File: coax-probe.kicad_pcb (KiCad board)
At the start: 2 copper layers, 37.3 x 21 mm, 34 parts, among them J1 Conn_01x02, J2 Conn_Coaxial, J3 Conn_01x02, J4 Conn_01x03, J5 Conn_Coaxial, J6 Conn_01x02, U1 OPA690, U2 INA128, U3 OPA690, U4 CJ431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

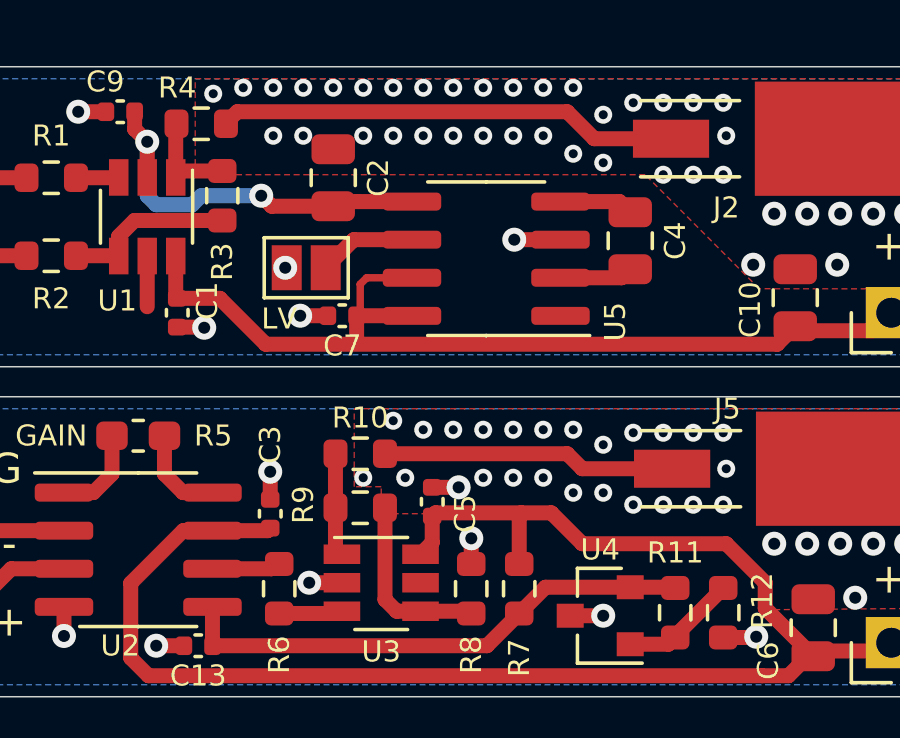
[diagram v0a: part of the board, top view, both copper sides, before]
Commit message: Fix 50-ohm trace width
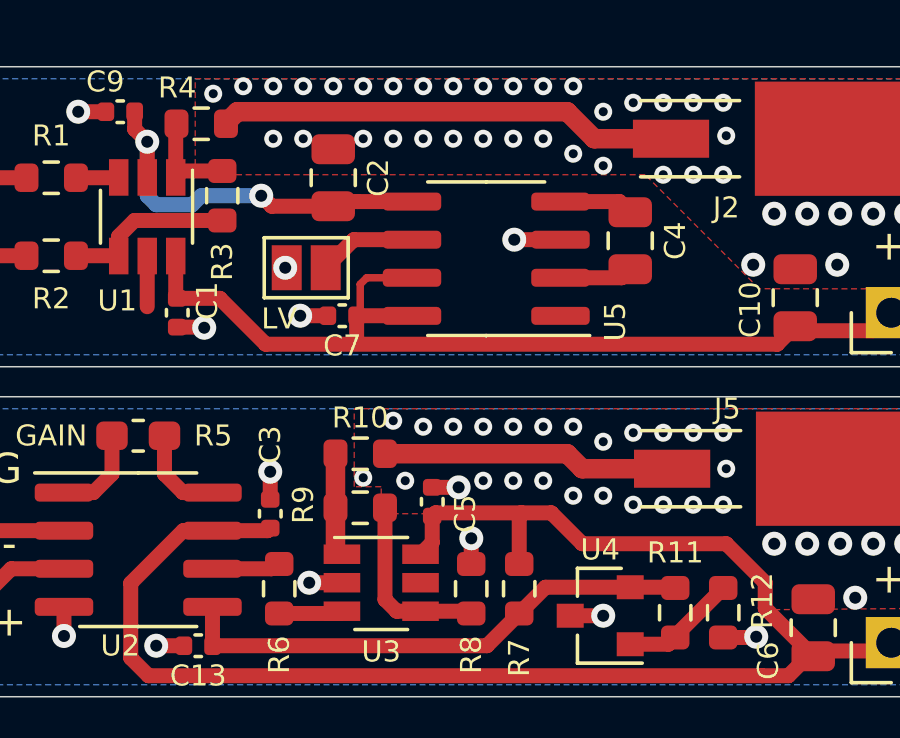
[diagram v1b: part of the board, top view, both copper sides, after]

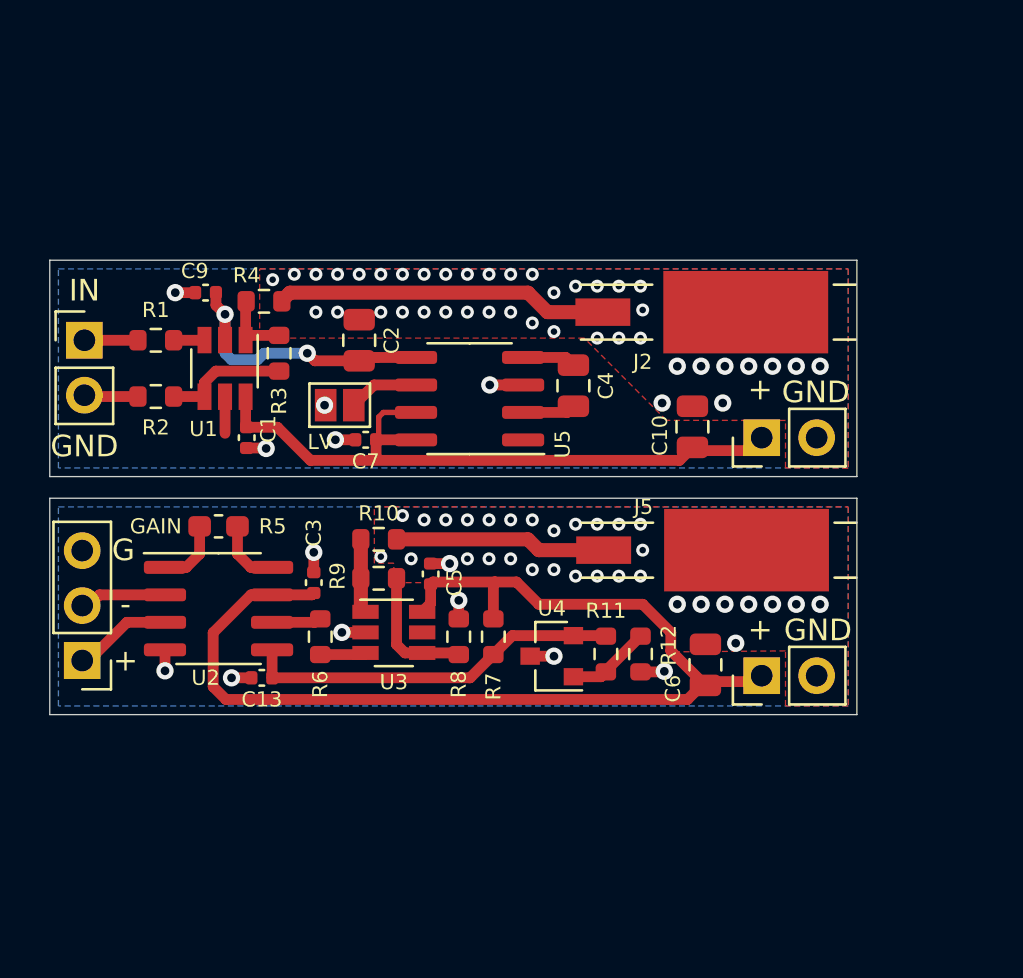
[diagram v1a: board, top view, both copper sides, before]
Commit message: Use SMA connectors
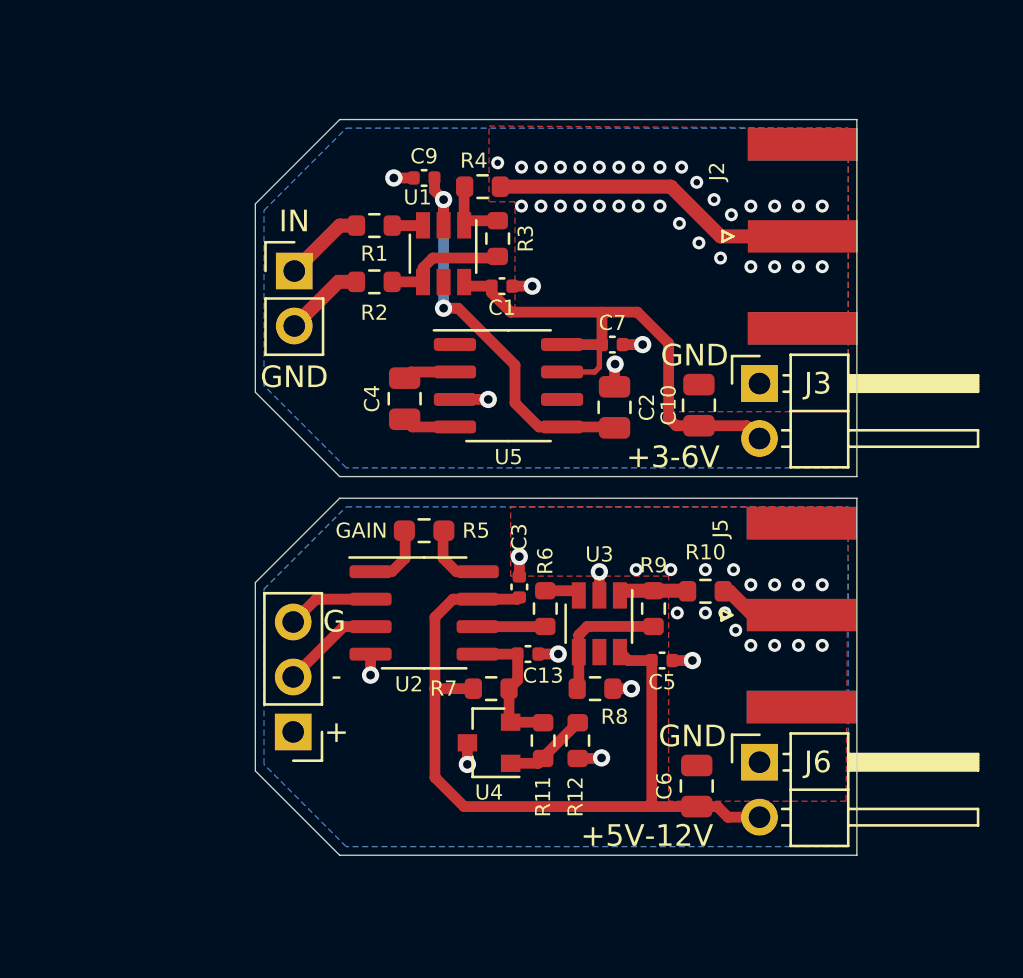
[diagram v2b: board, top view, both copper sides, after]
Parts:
- removed JP1: LV, Jumper:SolderJumper-2_P1.3mm_Open_Pad1.0x1.5mm
- J2, J5: value Conn_Coaxial -> SMA; footprint Beck:Coax_Cable_Solder -> Connector_Coaxial:SMA_Amphenol_132289_EdgeMount
- J3, J6: footprint Connector_PinHeader_2.54mm:PinHeader_1x02_P2.54mm_Vertical -> Connector_PinHeader_2.54mm:PinHeader_1x02_P2.54mm_Horizontal
- R12: value - -> DNP
- R5: value - -> DNP; footprint Capacitor_SMD:C_0603_1608Metric_Pad1.05x0.95mm_HandSolder -> Resistor_SMD:R_0603_1608Metric_Pad0.98x0.95mm_HandSolder
- moved R10 15.3 mm to (178.0, 75.3)
- moved C1 13.7 mm to (168.6, 61.2), turned to 0 degrees
- moved R9 12.8 mm to (175.6, 76.1), turned to 270 degrees
- moved C13 12.3 mm to (169.8, 78.2), turned to 0 degrees
- moved C7 12.2 mm to (173.7, 63.9), turned to 0 degrees
- moved C2 12.2 mm to (173.8, 66.8)
- moved C5 11.4 mm to (176.0, 78.5), turned to 0 degrees
- moved R1 11.4 mm to (162.7, 58.4)
- moved C9 11.4 mm to (165.0, 56.2)
- moved R2 11.4 mm to (162.7, 61.0)
- moved R3 11.4 mm to (168.4, 59.0)
- moved R4 11.4 mm to (167.7, 56.6)
- moved U1 11.4 mm to (165.9, 59.7)
- moved R6 10.5 mm to (170.6, 76.1), turned to 270 degrees
- moved J4 10.3 mm to (158.9, 81.8)
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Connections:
- J3 pad 1: VCC -> GND
- J3 pad 2: GND -> VCC
- J4 pad 1: /IN+ -> GND
- J4 pad 2: /IN- -> /IN+
- J4 pad 3: GND -> /IN-
- J6 pad 1: VCC -> GND
- J6 pad 2: GND -> VCC
- U5 pad 6: Net-(JP1-Pad1) -> (no net)
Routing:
- net VCC: track 84.4 -> 62.3 mm
- net REF: track 17.5 -> 6.70 mm
- net /OUTD: track 9.44 -> 4.08 mm
- net VSS: track 13.3 -> 18.6 mm
- net Net-(JP1-Pad1): track 3.26 -> 0.00 mm
- net GND: track 14.6 -> 16.9 mm, vias 87 -> 61
- net (no net): track 1.69 -> 0.00 mm
- net Net-(J1-Pad1): track 2.47 -> 3.74 mm
- net /INA: track 2.19 -> 3.13 mm
- net /OUT: track 15.5 -> 14.9 mm
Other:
- board size 37.3 x 21 mm -> 27.8 x 34 mm
- board text added: "220MHz 50Ω 1X Active Probe"
- board text added: "Active Differential Probe 1.2MHz (G=1) 50Ω"
- board text removed: "1.2MHz (G=1) 50Ω Active Differential Probe"
- board text removed: "2.5V−6V"
- board text removed: "220MHz 50Ω Active Probe"
- board text removed: "5V−12V"
- board text removed: "Solder LV for <3V"

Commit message: Tweak zones.
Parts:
- moved C10 0.20 mm to (177.5, 66.7)

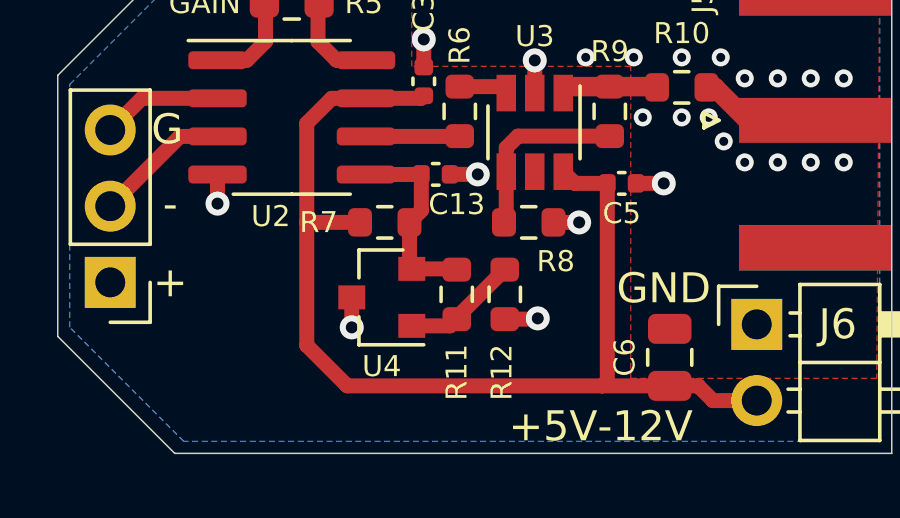
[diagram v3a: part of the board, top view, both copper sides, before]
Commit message: Space out Vref more
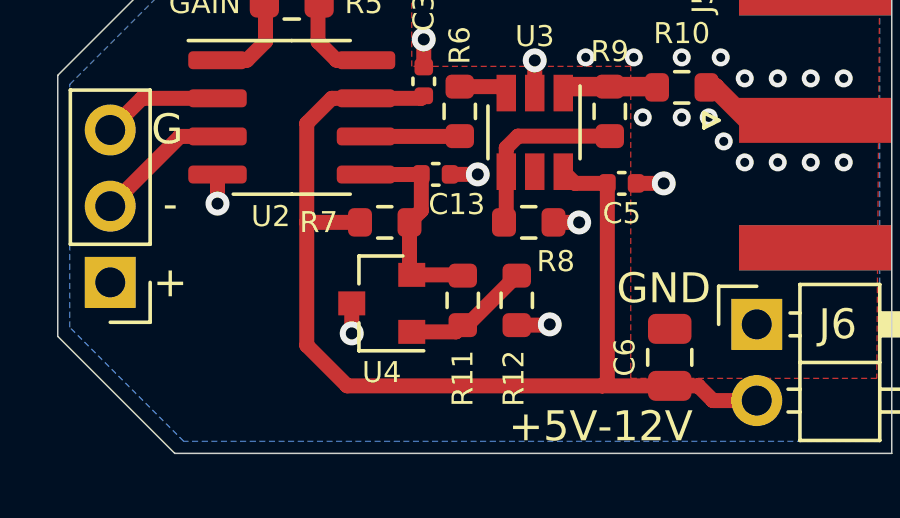
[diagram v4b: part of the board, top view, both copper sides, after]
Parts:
- moved R12 0.45 mm to (172.5, 82.4)
- moved R11 0.28 mm to (170.7, 82.4)
- moved U4 0.20 mm to (168.0, 82.5)
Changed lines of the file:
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@@
     (thickness 1.6)
     (drawings 28)
-    (tracks 190)
+    (tracks 191)
     (zones 0)
     (modules 33)
@@
   )
   (module Resistor_SMD:R_0603_1608Metric (layer F.Cu)
-    (at 172.1 82.2 270)
+    (at 172.5 82.4 270)
     (descr "Resistor SMD 0603 (1608 Metric), square (rectangular) end terminal, IPC_7351 nominal, (Body size source: IPC-SM-782 page 72, https://www.pcb-3d.com/wordpress/wp-content/uploads/ipc-sm-782a_amendment_1_and_2.pdf), generated with kicad-footprint-generator")
     (tags resistor)
@@
   )
   (module Resistor_SMD:R_0603_1608Metric (layer F.Cu)
-    (at 170.5 82.2 270)
+    (at 170.7 82.4 270)
     (descr "Resistor SMD 0603 (1608 Metric), square (rectangular) end terminal, IPC_7351 nominal, (Body size source: IPC-SM-782 page 72, https://www.pcb-3d.com/wordpress/wp-content/uploads/ipc-sm-782a_amendment_1_and_2.pdf), generated with kicad-footprint-generator")
     (tags resistor)
@@
   )
   (module Package_TO_SOT_SMD:SOT-23 (layer F.Cu)
-    (at 168 82.3 180)
+    (at 168 82.5 180)
     (descr "SOT-23, Standard")
     (tags SOT-23)
@@
   (via (at 173.1 74.399998) (size 0.8) (drill 0.4) (layers F.Cu B.Cu) (net 1))
   (segment (start 173.1 75.49) (end 173.1 74.399998) (width 0.5) (layer F.Cu) (net 1))
-  (via (at 173.2 83) (size 0.8) (drill 0.4) (layers F.Cu B.Cu) (net 1))
-  (segment (start 172.1 83.025) (end 173.175 83.025) (width 0.5) (layer F.Cu) (net 1))
+  (via (at 173.6 83.2) (size 0.8) (drill 0.4) (layers F.Cu B.Cu) (net 1))
+  (segment (start 172.5 83.225) (end 173.575 83.225) (width 0.5) (layer F.Cu) (net 1))
   (via (at 174.579986 79.801971) (size 0.8) (drill 0.4) (layers F.Cu B.Cu) (net 1))
   (segment (start 173.725 79.8) (end 174.578015 79.8) (width 0.5) (layer F.Cu) (net 1))
@@
   (via (at 171.2 78.2) (size 0.8) (drill 0.4) (layers F.Cu B.Cu) (net 1))
   (segment (start 170.28 78.2) (end 171.2 78.2) (width 0.5) (layer F.Cu) (net 1))
-  (via (at 167 83.29999) (size 0.8) (drill 0.4) (layers F.Cu B.Cu) (net 1))
-  (segment (start 167 82.3) (end 167 83.29999) (width 0.5) (layer F.Cu) (net 1))
+  (via (at 167 83.49999) (size 0.8) (drill 0.4) (layers F.Cu B.Cu) (net 1))
+  (segment (start 167 82.5) (end 167 83.49999) (width 0.5) (layer F.Cu) (net 1))
   (via (at 177.4 78.5) (size 0.8) (drill 0.4) (layers F.Cu B.Cu) (net 1))
   (segment (start 176.48 78.5) (end 177.4 78.5) (width 0.5) (layer F.Cu) (net 1))
@@
   (segment (start 170.59 76.935) (end 170.6 76.925) (width 0.5) (layer F.Cu) (net 13))
   (segment (start 167.475 76.935) (end 170.59 76.935) (width 0.5) (layer F.Cu) (net 13))
-  (segment (start 170.475 81.35) (end 170.5 81.375) (width 0.5) (layer F.Cu) (net 14))
-  (segment (start 169 81.35) (end 170.475 81.35) (width 0.5) (layer F.Cu) (net 14))
+  (segment (start 170.675 81.55) (end 170.7 81.575) (width 0.5) (layer F.Cu) (net 14))
+  (segment (start 169.2 81.55) (end 170.675 81.55) (width 0.5) (layer F.Cu) (net 14))
   (segment (start 169.315 78.205) (end 169.32 78.2) (width 0.5) (layer F.Cu) (net 14))
   (segment (start 167.475 78.205) (end 169.315 78.205) (width 0.5) (layer F.Cu) (net 14))
-  (segment (start 168.925 81.275) (end 169 81.35) (width 0.5) (layer F.Cu) (net 14))
-  (segment (start 168.925 79.8) (end 168.925 81.275) (width 0.5) (layer F.Cu) (net 14))
+  (segment (start 168.925 81.475) (end 169 81.55) (width 0.5) (layer F.Cu) (net 14))
+  (segment (start 168.925 80) (end 168.925 81.475) (width 0.5) (layer F.Cu) (net 14))
   (segment (start 169.32 79.405) (end 168.925 79.8) (width 0.5) (layer F.Cu) (net 14))
   (segment (start 169.32 78.2) (end 169.32 79.405) (width 0.5) (layer F.Cu) (net 14))
@@
   (segment (start 171.935 75.275) (end 172.15 75.49) (width 0.5) (layer F.Cu) (net 16))
   (segment (start 170.6 75.275) (end 171.935 75.275) (width 0.5) (layer F.Cu) (net 16))
-  (segment (start 170.275 83.25) (end 170.5 83.025) (width 0.5) (layer F.Cu) (net 17))
-  (segment (start 169 83.25) (end 170.275 83.25) (width 0.5) (layer F.Cu) (net 17))
-  (segment (start 170.5 82.975) (end 172.1 81.375) (width 0.5) (layer F.Cu) (net 17))
-  (segment (start 170.5 83.025) (end 170.5 82.975) (width 0.5) (layer F.Cu) (net 17))
+  (segment (start 170.475 83.45) (end 170.7 83.225) (width 0.5) (layer F.Cu) (net 17))
+  (segment (start 169.2 83.45) (end 170.475 83.45) (width 0.5) (layer F.Cu) (net 17))
+  (segment (start 170.7 83.225) (end 170.7 83.175) (width 0.5) (layer F.Cu) (net 17))
+  (segment (start 170.85 83.225) (end 172.5 81.575) (width 0.5) (layer F.Cu) (net 17))
+  (segment (start 170.7 83.225) (end 170.85 83.225) (width 0.5) (layer F.Cu) (net 17))
   (segment (start 164.455 67.704999) (end 164.1 67.35) (width 0.5) (layer F.Cu) (net 18))
   (segment (start 166.425 67.705) (end 164.455 67.704999) (width 0.5) (layer F.Cu) (net 18))

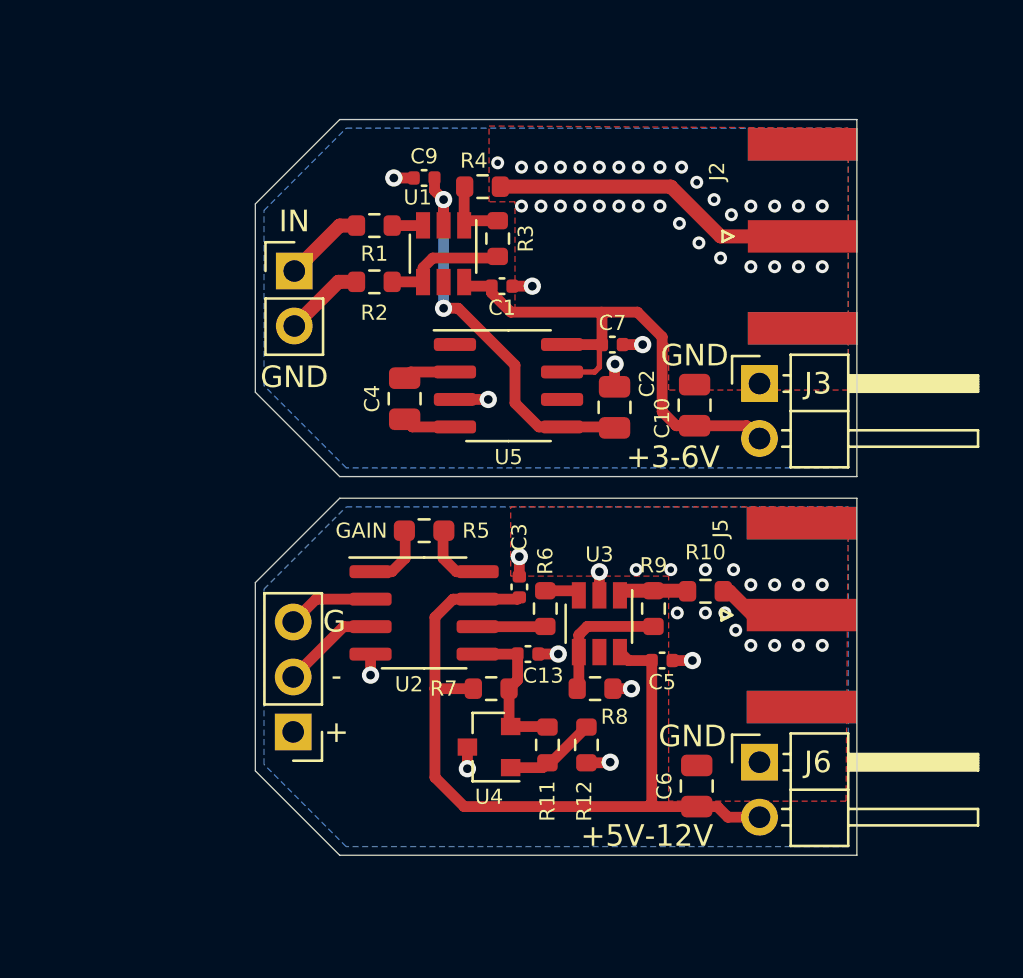
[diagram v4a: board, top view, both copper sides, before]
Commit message: Widen PCBs for JLC assembly service
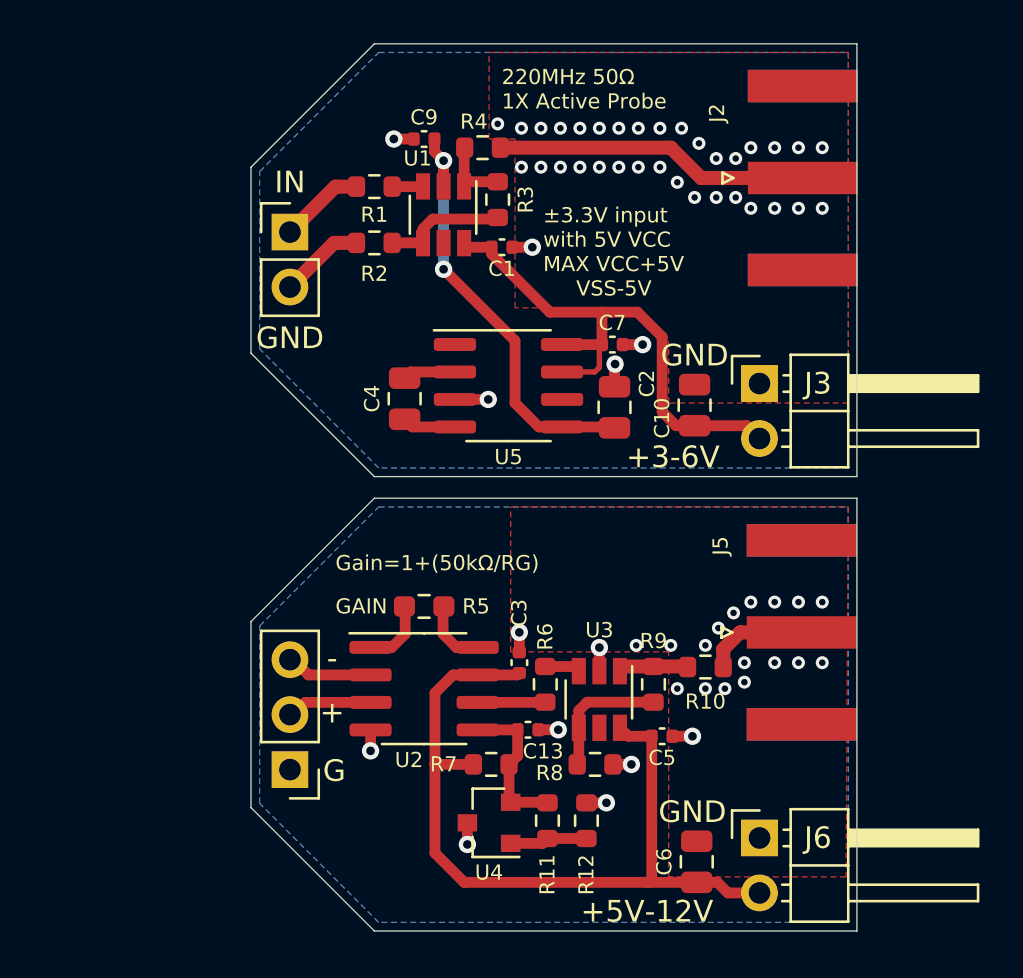
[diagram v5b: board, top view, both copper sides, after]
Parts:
- moved C13 3.50 mm to (169.8, 81.7)
- moved C3 3.50 mm to (169.4, 78.6)
- moved C5 3.50 mm to (176.0, 82.0)
- moved C6 3.50 mm to (177.6, 87.8)
- moved J6 3.50 mm to (180.5, 86.7)
- moved R10 3.50 mm to (178.0, 78.8)
- moved R11 3.50 mm to (170.7, 85.9)
- moved R12 3.50 mm to (172.5, 85.9), turned to 90 degrees
- moved R5 3.50 mm to (165.0, 76.0)
- moved R6 3.50 mm to (170.6, 79.6)
- moved R7 3.50 mm to (168.1, 83.3)
- moved R8 3.50 mm to (172.9, 83.3)
- moved R9 3.50 mm to (175.6, 79.6)
- moved U2 3.50 mm to (165.0, 79.8)
- moved U3 3.50 mm to (173.1, 80.3)
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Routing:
- net VSS: track 18.6 -> 20.0 mm
- net VCC: track 62.3 -> 63.1 mm
- net /IN+: track 4.54 -> 3.81 mm
- net /OUTD: track 4.08 -> 4.77 mm
- net Net-(R11-Pad2): track 4.13 -> 3.44 mm
- net GND: vias 61 -> 63
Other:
- board size 27.8 x 34 mm -> 28 x 41 mm
- board text added: "Gain=1+(50kΩ/RG)"
- board text added: "ICM: -2V−VCC+2V MAX: ±40V to GND"
- board text removed: "Gain=1+(50kΩ/RG) ICM: -2V−VCC+2V MAX: ±40V to GND"
